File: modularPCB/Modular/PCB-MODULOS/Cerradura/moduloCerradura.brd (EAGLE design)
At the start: 38 x 33 mm, 8 parts

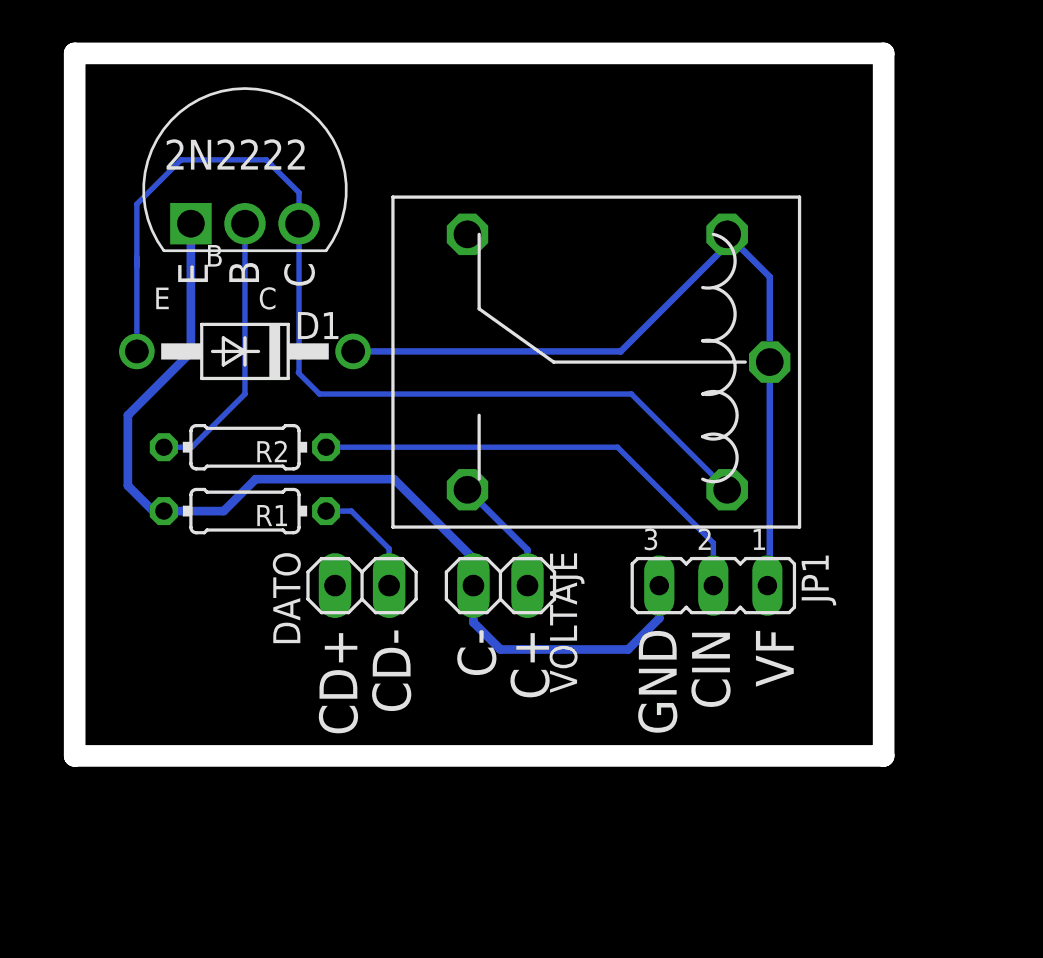
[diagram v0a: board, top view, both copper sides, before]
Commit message: Se agregaron brd de la ultima actualización
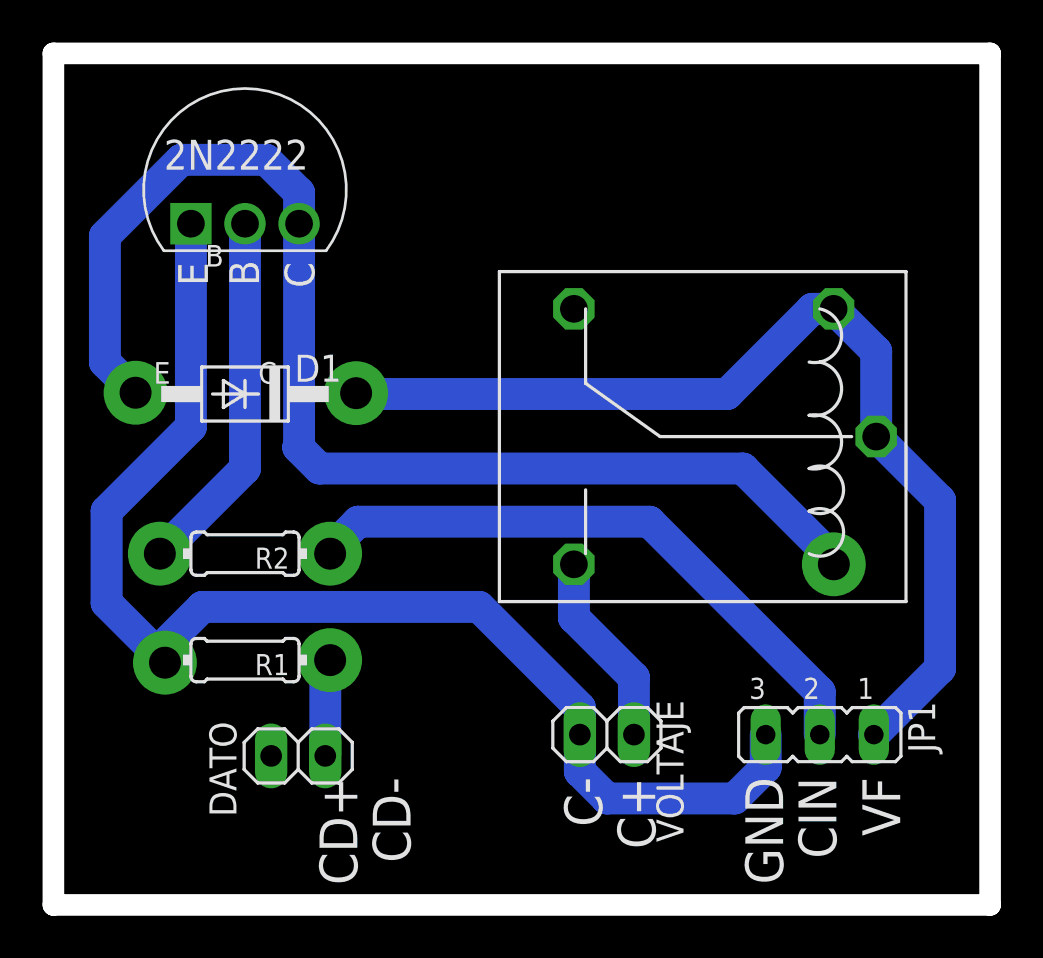
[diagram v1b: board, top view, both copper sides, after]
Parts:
- moved JP1 8.60 mm to (35.0, 1.00)
- moved VOLTAJE 8.60 mm to (25.0, 1.00)
- moved DATO 8.54 mm to (10.5, 0.00)
- moved R1 7.00 mm to (8.00, 4.50)
- moved U$2 6.10 mm to (29.5, 15.0)
- moved R2 5.00 mm to (8.00, 9.50)
- moved D1 2.00 mm to (8.00, 17.0)
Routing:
- net GND: track 46.8 -> 60.6 mm
- net N$2: track 47.4 -> 58.8 mm
- net VF: track 37.5 -> 47.6 mm
- net PULSO-CHAPA: track 22.1 -> 29.1 mm
- net N$1: track 12.8 -> 17.1 mm
- net N$3: track 5.67 -> 9.17 mm
- net DATO-CHAPA: track 5.42 -> 4.52 mm
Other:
- board size 38 x 33 mm -> 44 x 40 mm
